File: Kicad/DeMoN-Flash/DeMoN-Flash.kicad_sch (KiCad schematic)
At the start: 37 parts, among them CN1 ECC43DCAI-S189, Q1 ZVP2106A, Q2 ZVP2106A, SW1 SW_Push, SW2 SW_Wuerth_450301014042, U1 GAL16V8, U10 IS61C5128AS-25QLI, U11 MC1455B, U2 GAL16V8, U3 GAL16V8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

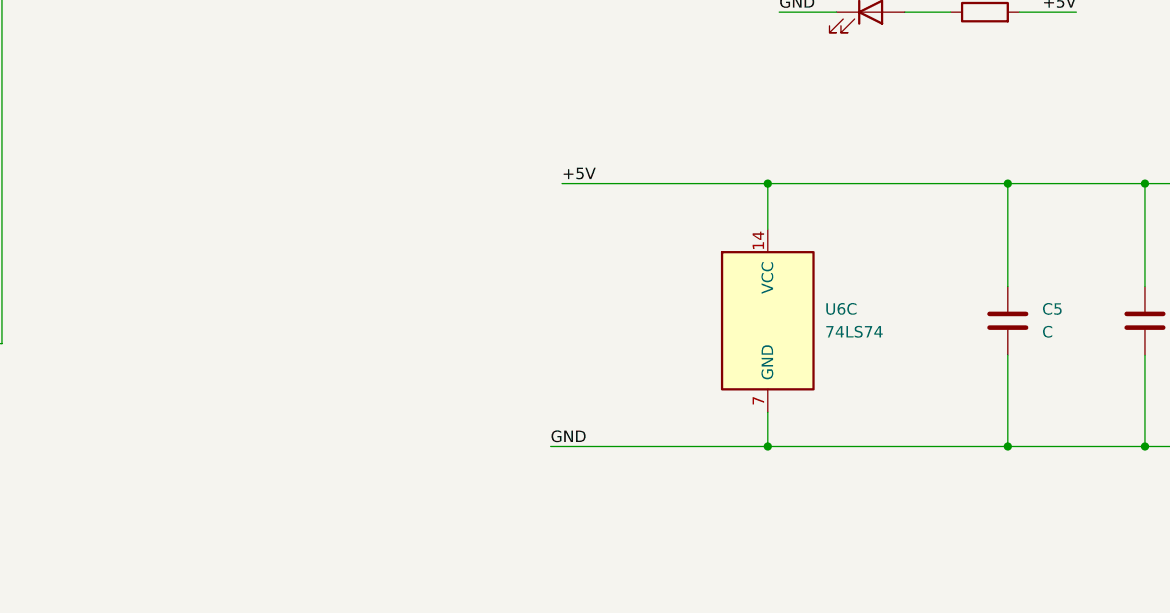
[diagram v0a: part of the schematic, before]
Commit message: added some decoupling cap
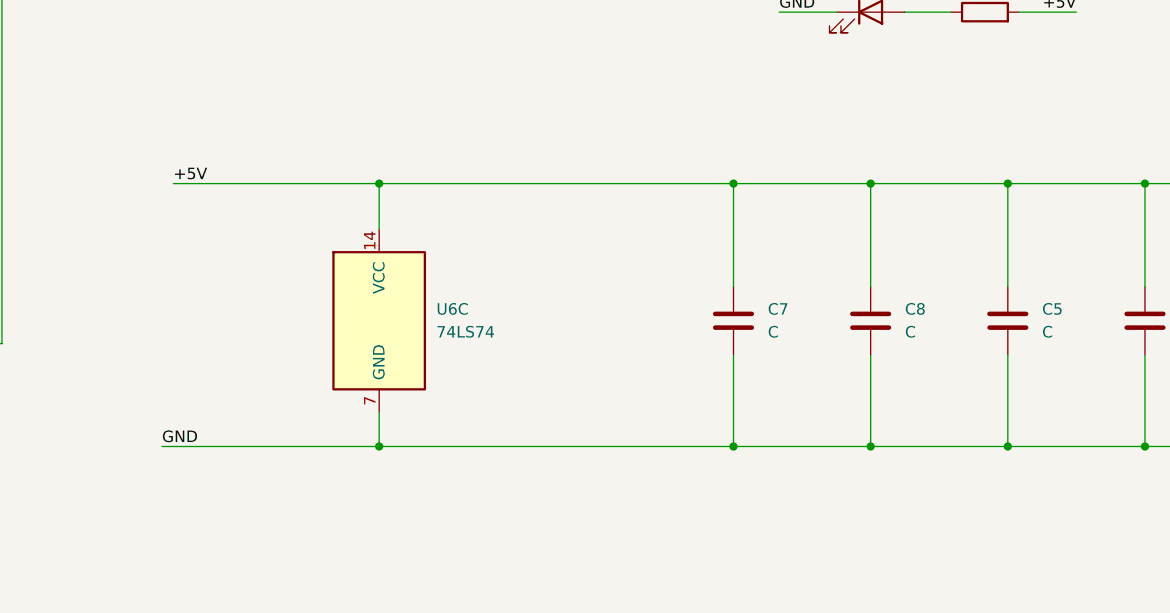
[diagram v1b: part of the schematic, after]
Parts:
- added C7, C8: C, Capacitor_SMD:C_1206_3216Metric_Pad1.33x1.80mm_HandSolder, symbol Device:C
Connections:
- net +5V: now also C7.1, C8.1
- net GND: now also C7.2, C8.2
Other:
- moved on the sheet: U6C
